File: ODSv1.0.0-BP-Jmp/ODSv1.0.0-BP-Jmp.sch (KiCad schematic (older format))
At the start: 4 parts

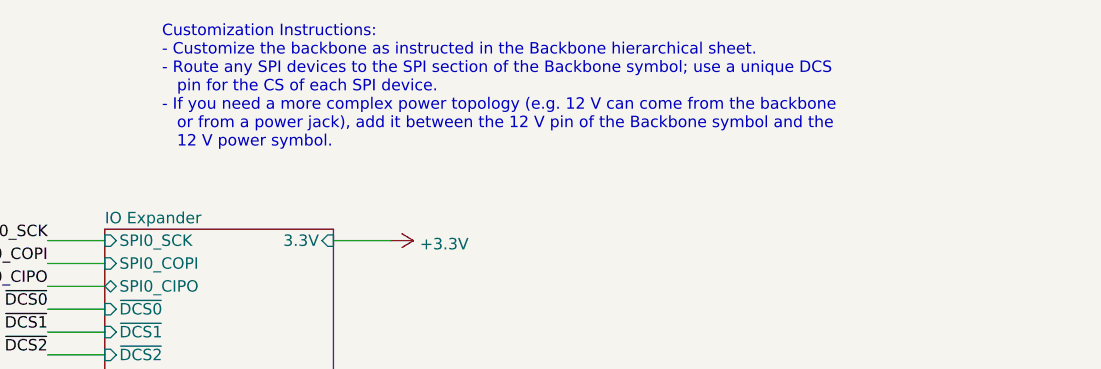
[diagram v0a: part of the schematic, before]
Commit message: Fix implementation of SPI CS multiplexing system (#22)
* Disconnect PP-T41's MAX7317's DOUT, since it's not needed anyways (#16)

* Disconnect BT & BP-Jmp backbone MAX7317 DOUT (#16); make DOUT output pin

* Replace DAC with a second MAX7317 expander with pullup resistors

* Insert 3-state buffers between MAX7317 DOUTs and CIPO in BP-Jmp (#16)

* Update symbol fields for I/O expansion components in BP-Jmp

* Consolidate free space by moving the AD7689 chip

* Add pull-ups on demuxed DCS (#17), move pull-ups to bottom of BP-Jmp

* Insert 3-state buffers between all MAX7317 DOUTs and CIPO (#16)

* Add bypass caps to the 3-state buffers for BP-Jmp's I/O expanders

* Fix title block for SPI DCS Selector sheet in BP-Jmp

* Use 2k pullups instead of 20k pullups on BP-Jmp

* Add 2k pullups on demuxed DSCS pins in PP-T41

* Define a NoPufferfish BOM variant of PP-T41

* Adjust the 12V copper fills on PP-T41

* Add 2k pullups within the DSCS selector in PP-T41 (#17)

* Add more information to READMEs

* Add 2k pullups within DCS selectors (#17), bump BP-Jmp to 0.2.0

* Fix errors in PR template for modified boards

* Move usage on I/O peripherals into a subsection in BP-Jmp's README.md

* Update KiCad preview & mechanical renders of all boards

* Improve & consolidate pull request templates

* Update raytrace renders of the entire stack

* Add missing definition for NoPufferfish variant for PP-T41

* Add link to CADLab project for this repo

* Remove the message annoyingly added by CADLab to top of README.md
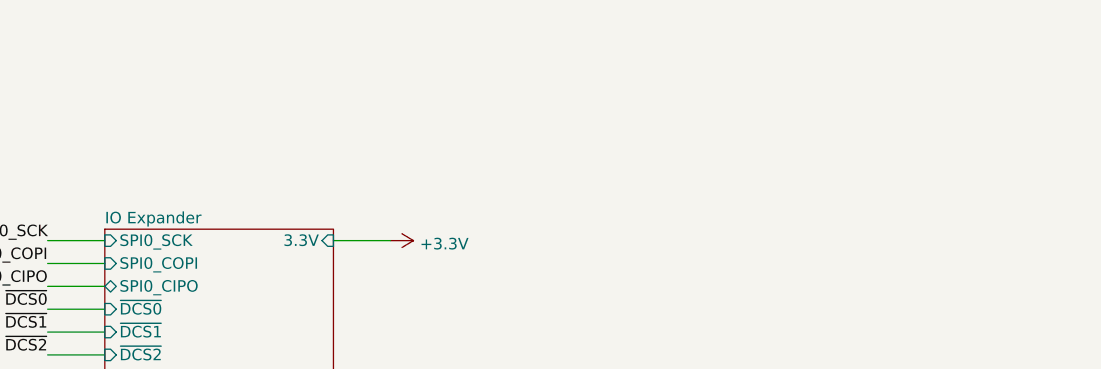
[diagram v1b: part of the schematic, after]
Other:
- note removed: "Customization Instructions:\n- Customize the backbone as instructed in the Backbone hierarchical sheet.\n- Route any SPI devices to the SPI section of the Backbone symbol; use a unique DCS\n pin for the CS of each SPI device.\n- If you need a more complex power topology (e.g. 12 V can come from the backbone\n or from a power jack), add it between the 12 V pin of the Backbone symbol and the\n 12 V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"
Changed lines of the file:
@@
 Sheet 1 9
 Title "Breakout Plane for Jumper Wires"
-Date "2021-03-09"
-Rev "v0.1.1"
+Date "2021-03-11"
+Rev "v0.2.0"
 Comp "Prakash Lab/Octopi Team"
 Comment1 "Designer: Ethan Li"
@@
 	0    1    1    0
 $EndComp
-Text Notes 7000 1100 0    50   ~ 0
-Customization Instructions:\n- Customize the backbone as instructed in the Backbone hierarchical sheet.\n- Route any SPI devices to the SPI section of the Backbone symbol; use a unique DCS\n   pin for the CS of each SPI device.\n- If you need a more complex power topology (e.g. 12 V can come from the backbone\n   or from a power jack), add it between the 12 V pin of the Backbone symbol and the\n   12 V power symbol.
 $Comp
 L Mechanical:MountingHole H1
